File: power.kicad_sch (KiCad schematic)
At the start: 44 parts, among them J1 KYCON_KPJX-4S-S, J2 MicroFit_2x02, J3 24V/5A OUT, J3B1 DNI, Q1 BC847, Q2 IRF9540SPBF, Q3 BC857, SW1 DNI, U1 MC78M12CDT-TR, U2 MAX5035BUSA

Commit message: WIP
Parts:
- D3, D4, D5: value 1N5819WS -> SDM20U40; footprint -Project:D_SOD-323_DOT -> Diode_SMD:D_SOD-523; JLCMFR# 1N5819WS -> SDM20U40-7; JLCMOQ 5 -> 15; JLCPART C191023 -> C139439
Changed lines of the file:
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@@
     (pin "3")
+  )
+  (symbol (lib_id "Device:D_Schottky") (at 91.44 124.46 0) (mirror x) (unit 1)
+    (in_bom yes) (on_board yes)
+    (property "Reference" "D5" (id 0) (at 91.44 121.92 0))
+    (property "Value" "SDM20U40" (id 1) (at 92.71 127 0))
+    (property "Footprint" "Diode_SMD:D_SOD-523" (id 2) (at 91.44 124.46 0)
+      (effects (font (size 1.27 1.27)) hide)
+    )
+    (property "Datasheet" "https://datasheet.lcsc.com/lcsc/1809192039_Diodes-Incorporated-SDM20U40-7_C139439.pdf" (id 3) (at 91.44 124.46 0)
+      (effects (font (size 1.27 1.27)) hide)
+    )
+    (property "JLCPART" "C139439" (id 4) (at 91.44 124.46 0)
+      (effects (font (size 1.27 1.27)) hide)
+    )
+    (property "JLCMFR#" "SDM20U40-7" (id 5) (at 91.44 124.46 0)
+      (effects (font (size 1.27 1.27)) hide)
+    )
+    (property "JLCMOQ" "15" (id 6) (at 91.44 124.46 0)
+      (effects (font (size 1.27 1.27)) hide)
+    )
+    (pin "1")
+    (pin "2")
   )
   (symbol (lib_id "Device:C") (at 228.6 96.52 90) (unit 1)
@@
     (pin "3")
   )
-  (symbol (lib_id "Device:D_Schottky") (at 69.85 64.77 0) (mirror y) (unit 1)
-    (in_bom yes) (on_board yes)
-    (property "Reference" "D3" (id 0) (at 69.85 62.23 0))
-    (property "Value" "1N5819WS" (id 1) (at 69.85 67.31 0))
-    (property "Footprint" "-Project:D_SOD-323_DOT" (id 2) (at 69.85 64.77 0)
-      (effects (font (size 1.27 1.27)) hide)
-    )
-    (property "Datasheet" "https://datasheet.lcsc.com/lcsc/1810202112_Guangdong-Hottech-1N5819WS_C191023.pdf" (id 3) (at 69.85 64.77 0)
-      (effects (font (size 1.27 1.27)) hide)
-    )
-    (property "LCSC" "" (id 4) (at 69.85 64.77 0)
-      (effects (font (size 1.27 1.27)) hide)
-    )
-    (property "JLCMFR#" "1N5819WS" (id 5) (at 69.85 64.77 0)
-      (effects (font (size 1.27 1.27)) hide)
-    )
-    (property "JLCMOQ" "5" (id 6) (at 69.85 64.77 0)
-      (effects (font (size 1.27 1.27)) hide)
-    )
-    (property "JLCPART" "C191023" (id 7) (at 69.85 64.77 0)
-      (effects (font (size 1.27 1.27)) hide)
-    )
-    (pin "1")
-    (pin "2")
-  )
   (symbol (lib_id "Device:R") (at 68.58 38.1 0) (unit 1)
     (in_bom yes) (on_board yes)
@@
     )
     (pin "1")
+  )
+  (symbol (lib_id "Device:D_Schottky") (at 85.09 118.11 270) (mirror x) (unit 1)
+    (in_bom yes) (on_board yes)
+    (property "Reference" "D4" (id 0) (at 87.63 115.57 90))
+    (property "Value" "SDM20U40" (id 1) (at 91.44 118.11 90))
+    (property "Footprint" "Diode_SMD:D_SOD-523" (id 2) (at 85.09 118.11 0)
+      (effects (font (size 1.27 1.27)) hide)
+    )
+    (property "Datasheet" "https://datasheet.lcsc.com/lcsc/1809192039_Diodes-Incorporated-SDM20U40-7_C139439.pdf" (id 3) (at 85.09 118.11 0)
+      (effects (font (size 1.27 1.27)) hide)
+    )
+    (property "JLCPART" "C139439" (id 4) (at 85.09 118.11 0)
+      (effects (font (size 1.27 1.27)) hide)
+    )
+    (property "JLCMFR#" "SDM20U40-7" (id 5) (at 85.09 118.11 0)
+      (effects (font (size 1.27 1.27)) hide)
+    )
+    (property "JLCMOQ" "15" (id 6) (at 85.09 118.11 0)
+      (effects (font (size 1.27 1.27)) hide)
+    )
+    (pin "1")
+    (pin "2")
   )
   (symbol (lib_id "Device:R") (at 55.88 57.15 0) (mirror x) (unit 1)
@@
     (pin "1")
   )
+  (symbol (lib_id "Device:D_Schottky") (at 69.85 64.77 0) (mirror y) (unit 1)
+    (in_bom yes) (on_board yes)
+    (property "Reference" "D3" (id 0) (at 69.85 62.23 0))
+    (property "Value" "SDM20U40" (id 1) (at 73.66 67.31 0))
+    (property "Footprint" "Diode_SMD:D_SOD-523" (id 2) (at 69.85 64.77 0)
+      (effects (font (size 1.27 1.27)) hide)
+    )
+    (property "Datasheet" "https://datasheet.lcsc.com/lcsc/1809192039_Diodes-Incorporated-SDM20U40-7_C139439.pdf" (id 3) (at 69.85 64.77 0)
+      (effects (font (size 1.27 1.27)) hide)
+    )
+    (property "JLCPART" "C139439" (id 4) (at 69.85 64.77 0)
+      (effects (font (size 1.27 1.27)) hide)
+    )
+    (property "JLCMFR#" "SDM20U40-7" (id 5) (at 69.85 64.77 0)
+      (effects (font (size 1.27 1.27)) hide)
+    )
+    (property "JLCMOQ" "15" (id 6) (at 69.85 64.77 0)
+      (effects (font (size 1.27 1.27)) hide)
+    )
+    (pin "1")
+    (pin "2")
+  )
   (symbol (lib_id "power:+5V") (at 271.78 98.425 0) (unit 1)
     (in_bom yes) (on_board yes)
@@
     )
     (pin "1")
-  )
-  (symbol (lib_id "Device:D_Schottky") (at 85.09 118.11 270) (mirror x) (unit 1)
-    (in_bom yes) (on_board yes)
-    (property "Reference" "D4" (id 0) (at 88.9 115.57 90))
-    (property "Value" "1N5819WS" (id 1) (at 91.44 118.11 90))
-    (property "Footprint" "-Project:D_SOD-323_DOT" (id 2) (at 85.09 118.11 0)
-      (effects (font (size 1.27 1.27)) hide)
-    )
-    (property "Datasheet" "https://datasheet.lcsc.com/lcsc/1810202112_Guangdong-Hottech-1N5819WS_C191023.pdf" (id 3) (at 85.09 118.11 0)
-      (effects (font (size 1.27 1.27)) hide)
-    )
-    (property "LCSC" "" (id 4) (at 85.09 118.11 0)
-      (effects (font (size 1.27 1.27)) hide)
-    )
-    (property "JLCMFR#" "1N5819WS" (id 5) (at 85.09 118.11 0)
-      (effects (font (size 1.27 1.27)) hide)
-    )
-    (property "JLCMOQ" "5" (id 6) (at 85.09 118.11 0)
-      (effects (font (size 1.27 1.27)) hide)
-    )
-    (property "JLCPART" "C191023" (id 7) (at 85.09 118.11 0)
-      (effects (font (size 1.27 1.27)) hide)
-    )
-    (pin "1")
-    (pin "2")
   )
   (symbol (lib_id "Regulator_Linear:L7812") (at 170.18 26.67 0) (unit 1)
@@
       (effects (font (size 1.27 1.27)) hide)
     )
-    (pin "1")
-    (pin "2")
-  )
-  (symbol (lib_id "Device:D_Schottky") (at 91.44 124.46 0) (mirror x) (unit 1)
-    (in_bom yes) (on_board yes)
-    (property "Reference" "D5" (id 0) (at 91.44 121.92 0))
-    (property "Value" "1N5819WS" (id 1) (at 92.71 127 0))
-    (property "Footprint" "-Project:D_SOD-323_DOT" (id 2) (at 91.44 124.46 0)
-      (effects (font (size 1.27 1.27)) hide)
-    )
-    (property "Datasheet" "https://datasheet.lcsc.com/lcsc/1810202112_Guangdong-Hottech-1N5819WS_C191023.pdf" (id 3) (at 91.44 124.46 0)
-      (effects (font (size 1.27 1.27)) hide)
-    )
-    (property "LCSC" "" (id 4) (at 91.44 124.46 0)
-      (effects (font (size 1.27 1.27)) hide)
-    )
-    (property "JLCMFR#" "1N5819WS" (id 5) (at 91.44 124.46 0)
-      (effects (font (size 1.27 1.27)) hide)
-    )
-    (property "JLCMOQ" "5" (id 6) (at 91.44 124.46 0)
-      (effects (font (size 1.27 1.27)) hide)
-    )
-    (property "JLCPART" "C191023" (id 7) (at 91.44 124.46 0)
-      (effects (font (size 1.27 1.27)) hide)
-    )

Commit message: Part supply references wip.
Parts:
- J1: JLCMFR# DNI -> Mouser:KPJX-4S-S
- J2: E14MFR# (none) -> 43045-0427; JLCMFR# DNI -> Mouser:43045-0427
- NT1, NT2, NT3: E14MFR# (none) -> DNI; JLCMFR# (none) -> DNI
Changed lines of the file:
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@@
+      (effects (font (size 1.27 1.27)) hide)
+    )
+    (property "E14MFR#" "DNI" (id 4) (at 60.96 124.46 0)
+      (effects (font (size 1.27 1.27)) hide)
+    )
+    (property "JLCMFR#" "DNI" (id 5) (at 60.96 124.46 0)
       (effects (font (size 1.27 1.27)) hide)
     )
@@
     )
     (property "Datasheet" "~" (id 3) (at 167.64 68.58 0)
+      (effects (font (size 1.27 1.27)) hide)
+    )
+    (property "E14MFR#" "DNI" (id 4) (at 167.64 68.58 0)
+      (effects (font (size 1.27 1.27)) hide)
+    )
+    (property "JLCMFR#" "DNI" (id 5) (at 167.64 68.58 0)
       (effects (font (size 1.27 1.27)) hide)
     )
@@
       (effects (font (size 1.27 1.27)) hide)
     )
-    (property "JLCMFR#" "DNI" (id 7) (at 36.83 35.56 0)
+    (property "JLCMFR#" "Mouser:KPJX-4S-S" (id 7) (at 36.83 35.56 0)
       (effects (font (size 1.27 1.27)) hide)
     )
@@
       (effects (font (size 1.27 1.27)) hide)
     )
+    (property "E14MFR#" "DNI" (id 4) (at 262.89 101.6 0)
+      (effects (font (size 1.27 1.27)) hide)
+    )
+    (property "JLCMFR#" "DNI" (id 5) (at 262.89 101.6 0)
+      (effects (font (size 1.27 1.27)) hide)
+    )
     (pin "1")
     (pin "2")
@@
       (effects (font (size 1.27 1.27)) hide)
     )
-    (property "JLCMFR#" "DNI" (id 7) (at 82.55 130.81 0)
-      (effects (font (size 1.27 1.27)) hide)
-    )
+    (property "JLCMFR#" "Mouser:43045-0427" (id 7) (at 82.55 130.81 0)
+      (effects (font (size 1.27 1.27)) hide)
+    )
+    (property "E14MFR#" "43045-0427" (id 8) (at 82.55 130.81 0)
+      (effects (font (size 1.27 1.27)) hide)
+    )

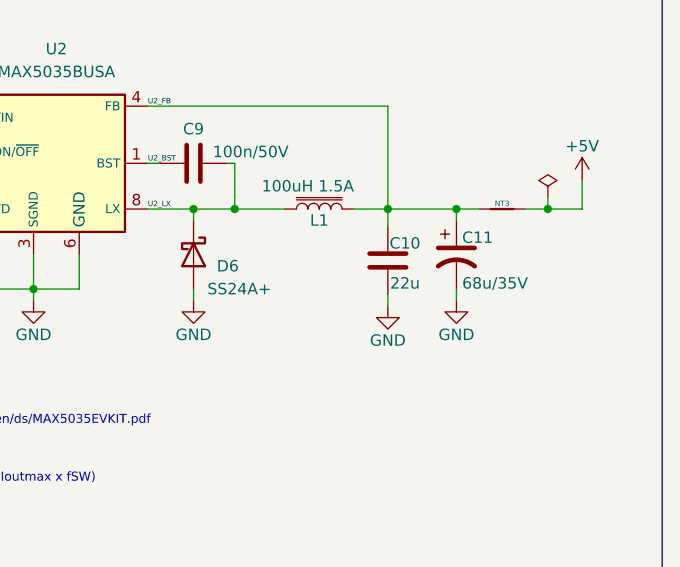
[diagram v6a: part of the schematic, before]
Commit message: WIP: Changing to terminal blocks for stepper, relay and VFD ports.
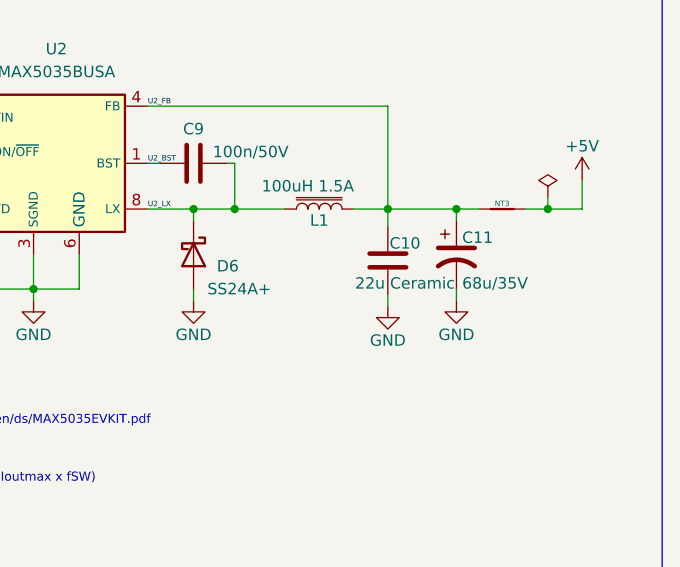
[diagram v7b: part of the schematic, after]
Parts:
- C10: value 22u -> 22u Ceramic
- R10: E14MFR# (none) -> MCSR06X1303FTL; E14PART 2073350 -> 2074189; JLCMFR# 0603WAF1003T5E -> 0603WAF1303T5E; JLCPART C25803 -> C22795
- R11, R2, R7: E14MFR# (none) -> MCMR06X1004FTL; E14PART (none) -> 2073351
- R12: E14MFR# (none) -> MCSR06X2203FTL; E14PART (none) -> 2074218; JLCMFR# 0603WAF1303T5E -> 0603WAF2203T5E; JLCPART C22795 -> C22961
- R4: E14MFR# (none) -> MCSR06X2203FTL; E14PART 2073350 -> 2074218
- R5: E14MFR# (none) -> MCSR06X1001FTL; E14PART 2447272 -> 2074166
- R6: E14MFR# (none) -> MCSR06X1303FTL; E14PART (none) -> 2074189
- R8: E14MFR# (none) -> MCSR06X6803FTL; E14PART 2073350 -> 2074298
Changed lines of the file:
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@@
       (effects (font (size 1.27 1.27)) hide)
     )
-    (property "E14PART" "2073350" (id 6) (at 68.58 38.1 0)
+    (property "E14PART" "2074218" (id 6) (at 68.58 38.1 0)
       (effects (font (size 1.27 1.27)) hide)
     )
@@
     )
     (property "JLCPART" "C22961" (id 9) (at 68.58 38.1 0)
+      (effects (font (size 1.27 1.27)) hide)
+    )
+    (property "E14MFR#" "MCSR06X2203FTL" (id 10) (at 68.58 38.1 0)
       (effects (font (size 1.27 1.27)) hide)
     )
@@
       (effects (font (size 1.27 1.27)) hide)
     )
-    (property "E14PART" "2073350" (id 6) (at 162.56 88.9 0)
-      (effects (font (size 1.27 1.27)) hide)
-    )
-    (property "JLCMFR#" "0603WAF1003T5E" (id 7) (at 162.56 88.9 0)
+    (property "E14PART" "2074189" (id 6) (at 162.56 88.9 0)
+      (effects (font (size 1.27 1.27)) hide)
+    )
+    (property "JLCMFR#" "0603WAF1303T5E" (id 7) (at 162.56 88.9 0)
       (effects (font (size 1.27 1.27)) hide)
     )
@@
       (effects (font (size 1.27 1.27)) hide)
     )
-    (property "JLCPART" "C25803" (id 9) (at 162.56 88.9 0)
+    (property "JLCPART" "C22795" (id 9) (at 162.56 88.9 0)
+      (effects (font (size 1.27 1.27)) hide)
+    )
+    (property "E14MFR#" "MCSR06X1303FTL" (id 10) (at 162.56 88.9 0)
       (effects (font (size 1.27 1.27)) hide)
     )
@@
       (effects (font (size 1.27 1.27)) hide)
     )
-    (property "E14PART" "" (id 6) (at 184.15 95.25 0)
+    (property "E14PART" "2073351" (id 6) (at 184.15 95.25 0)
       (effects (font (size 1.27 1.27)) hide)
     )
@@
     )
     (property "JLCPART" "C22935" (id 9) (at 184.15 95.25 0)
+      (effects (font (size 1.27 1.27)) hide)
+    )
+    (property "E14MFR#" "MCMR06X1004FTL" (id 10) (at 184.15 95.25 0)
       (effects (font (size 1.27 1.27)) hide)
     )
@@
       (effects (font (size 1.27 1.27)) hide)
     )
-    (property "E14PART" "" (id 6) (at 55.88 57.15 0)
+    (property "E14PART" "2073351" (id 6) (at 55.88 57.15 0)
       (effects (font (size 1.27 1.27)) hide)
     )
@@
     )
     (property "JLCPART" "C22935" (id 9) (at 55.88 57.15 0)
+      (effects (font (size 1.27 1.27)) hide)
+    )
+    (property "E14MFR#" "MCMR06X1004FTL" (id 10) (at 55.88 57.15 0)
       (effects (font (size 1.27 1.27)) hide)
     )
@@
       (effects (font (size 1.27 1.27)) hide)
     )
-    (property "E14PART" "" (id 6) (at 193.04 101.6 0)
-      (effects (font (size 1.27 1.27)) hide)
-    )
-    (property "JLCMFR#" "0603WAF1303T5E" (id 7) (at 193.04 101.6 0)
+    (property "E14PART" "2074218" (id 6) (at 193.04 101.6 0)
+      (effects (font (size 1.27 1.27)) hide)
+    )
+    (property "JLCMFR#" "0603WAF2203T5E" (id 7) (at 193.04 101.6 0)
       (effects (font (size 1.27 1.27)) hide)
     )
@@
       (effects (font (size 1.27 1.27)) hide)
     )
-    (property "JLCPART" "C22795" (id 9) (at 193.04 101.6 0)
+    (property "JLCPART" "C22961" (id 9) (at 193.04 101.6 0)
+      (effects (font (size 1.27 1.27)) hide)
+    )
+    (property "E14MFR#" "MCSR06X2203FTL" (id 10) (at 193.04 101.6 0)
       (effects (font (size 1.27 1.27)) hide)
     )
@@
       (effects (font (size 1.27 1.27)) hide)
     )
-    (property "E14PART" "2447272" (id 6) (at 69.85 124.46 0)
+    (property "E14PART" "2074166" (id 6) (at 69.85 124.46 0)
       (effects (font (size 1.27 1.27)) hide)
     )
@@
     )
     (property "JLCPART" "C21190" (id 9) (at 69.85 124.46 0)
+      (effects (font (size 1.27 1.27)) hide)
+    )
+    (property "E14MFR#" "MCSR06X1001FTL" (id 10) (at 69.85 124.46 0)
       (effects (font (size 1.27 1.27)) hide)
     )
@@
     (in_bom yes) (on_board yes)
     (property "Reference" "C10" (id 0) (at 252.095 105.41 0))
-    (property "Value" "22u" (id 1) (at 252.095 109.855 0))
+    (property "Value" "22u Ceramic" (id 1) (at 252.095 109.855 0))
     (property "Footprint" "Capacitor_SMD:C_1206_3216Metric" (id 2) (at 249.2248 103.505 0)
       (effects (font (size 1.27 1.27)) hide)
@@
       (effects (font (size 1.27 1.27)) hide)
     )
-    (property "E14PART" "" (id 6) (at 73.66 88.9 0)
+    (property "E14PART" "2074189" (id 6) (at 73.66 88.9 0)
       (effects (font (size 1.27 1.27)) hide)
     )
@@
     )
     (property "JLCPART" "C22795" (id 9) (at 73.66 88.9 0)
+      (effects (font (size 1.27 1.27)) hide)
+    )
+    (property "E14MFR#" "MCSR06X1303FTL" (id 10) (at 73.66 88.9 0)
       (effects (font (size 1.27 1.27)) hide)
     )
@@
       (effects (font (size 1.27 1.27)) hide)
     )
-    (property "E14PART" "2073350" (id 6) (at 85.09 43.18 0)
+    (property "E14PART" "2074298" (id 6) (at 85.09 43.18 0)
       (effects (font (size 1.27 1.27)) hide)
     )
@@
     )
     (property "JLCPART" "C25822" (id 9) (at 85.09 43.18 0)
+      (effects (font (size 1.27 1.27)) hide)
+    )
+    (property "E14MFR#" "MCSR06X6803FTL" (id 10) (at 85.09 43.18 0)
       (effects (font (size 1.27 1.27)) hide)
     )
@@
       (effects (font (size 1.27 1.27)) hide)
     )
-    (property "E14PART" "" (id 6) (at 85.09 33.02 0)
+    (property "E14PART" "2073351" (id 6) (at 85.09 33.02 0)
       (effects (font (size 1.27 1.27)) hide)
     )
@@
       (effects (font (size 1.27 1.27)) hide)
     )
+    (property "E14MFR#" "MCMR06X1004FTL" (id 10) (at 85.09 33.02 0)
+      (effects (font (size 1.27 1.27)) hide)
+    )
